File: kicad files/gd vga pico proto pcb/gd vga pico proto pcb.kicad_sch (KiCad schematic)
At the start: 58 parts, among them J1 RGB Bin, J2 CLKS, J3 SWD, J4 L77HDE15SD1CH4F, J5 VID_TXRX, J6 WIN, J7 5V, J8 USB_B_Micro, SW1 2040 RESET, U1 RP2040, U2 74HCT245, U3 74LVC2G04, U4 74LVC2G04, U5 MIC5504-3.3YM5, Y1 ECS-120-18-33-JEM-TR

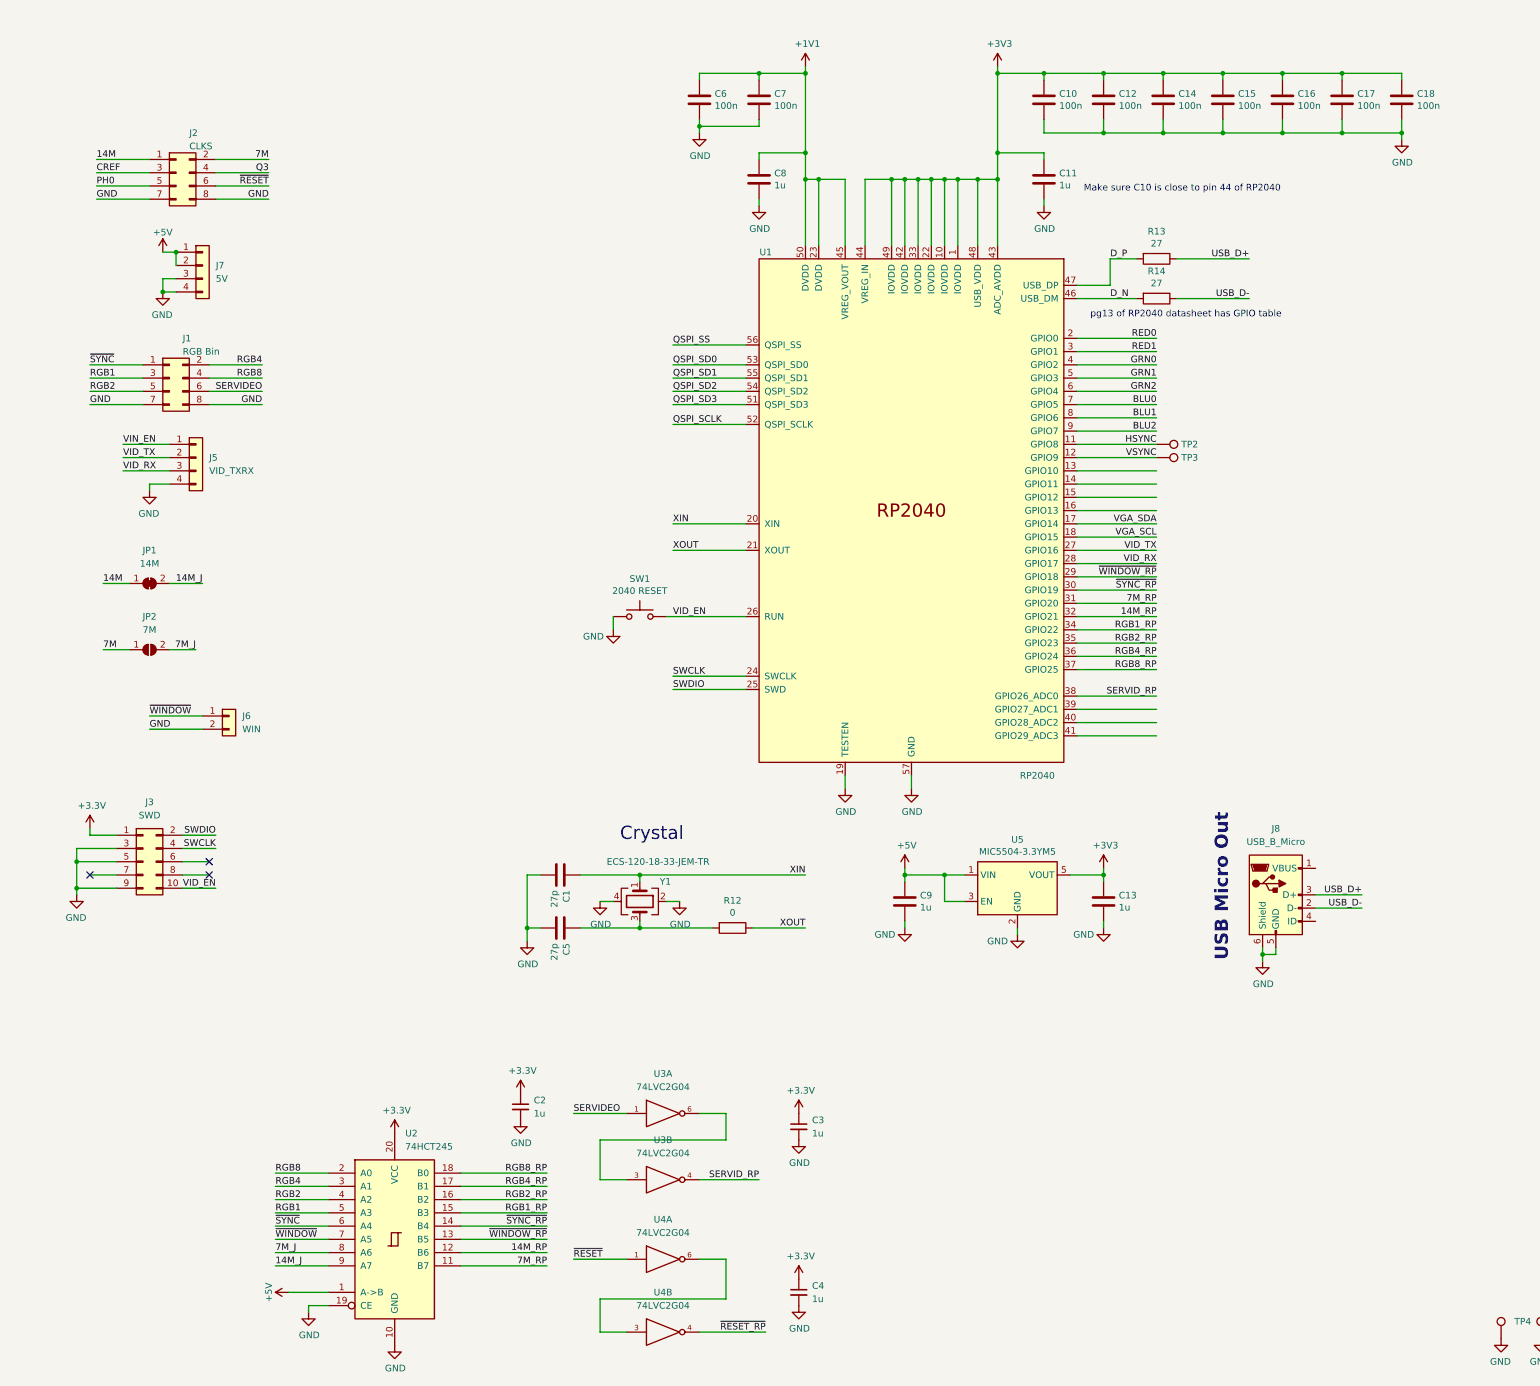
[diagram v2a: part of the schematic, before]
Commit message: post stream pixel pushing.
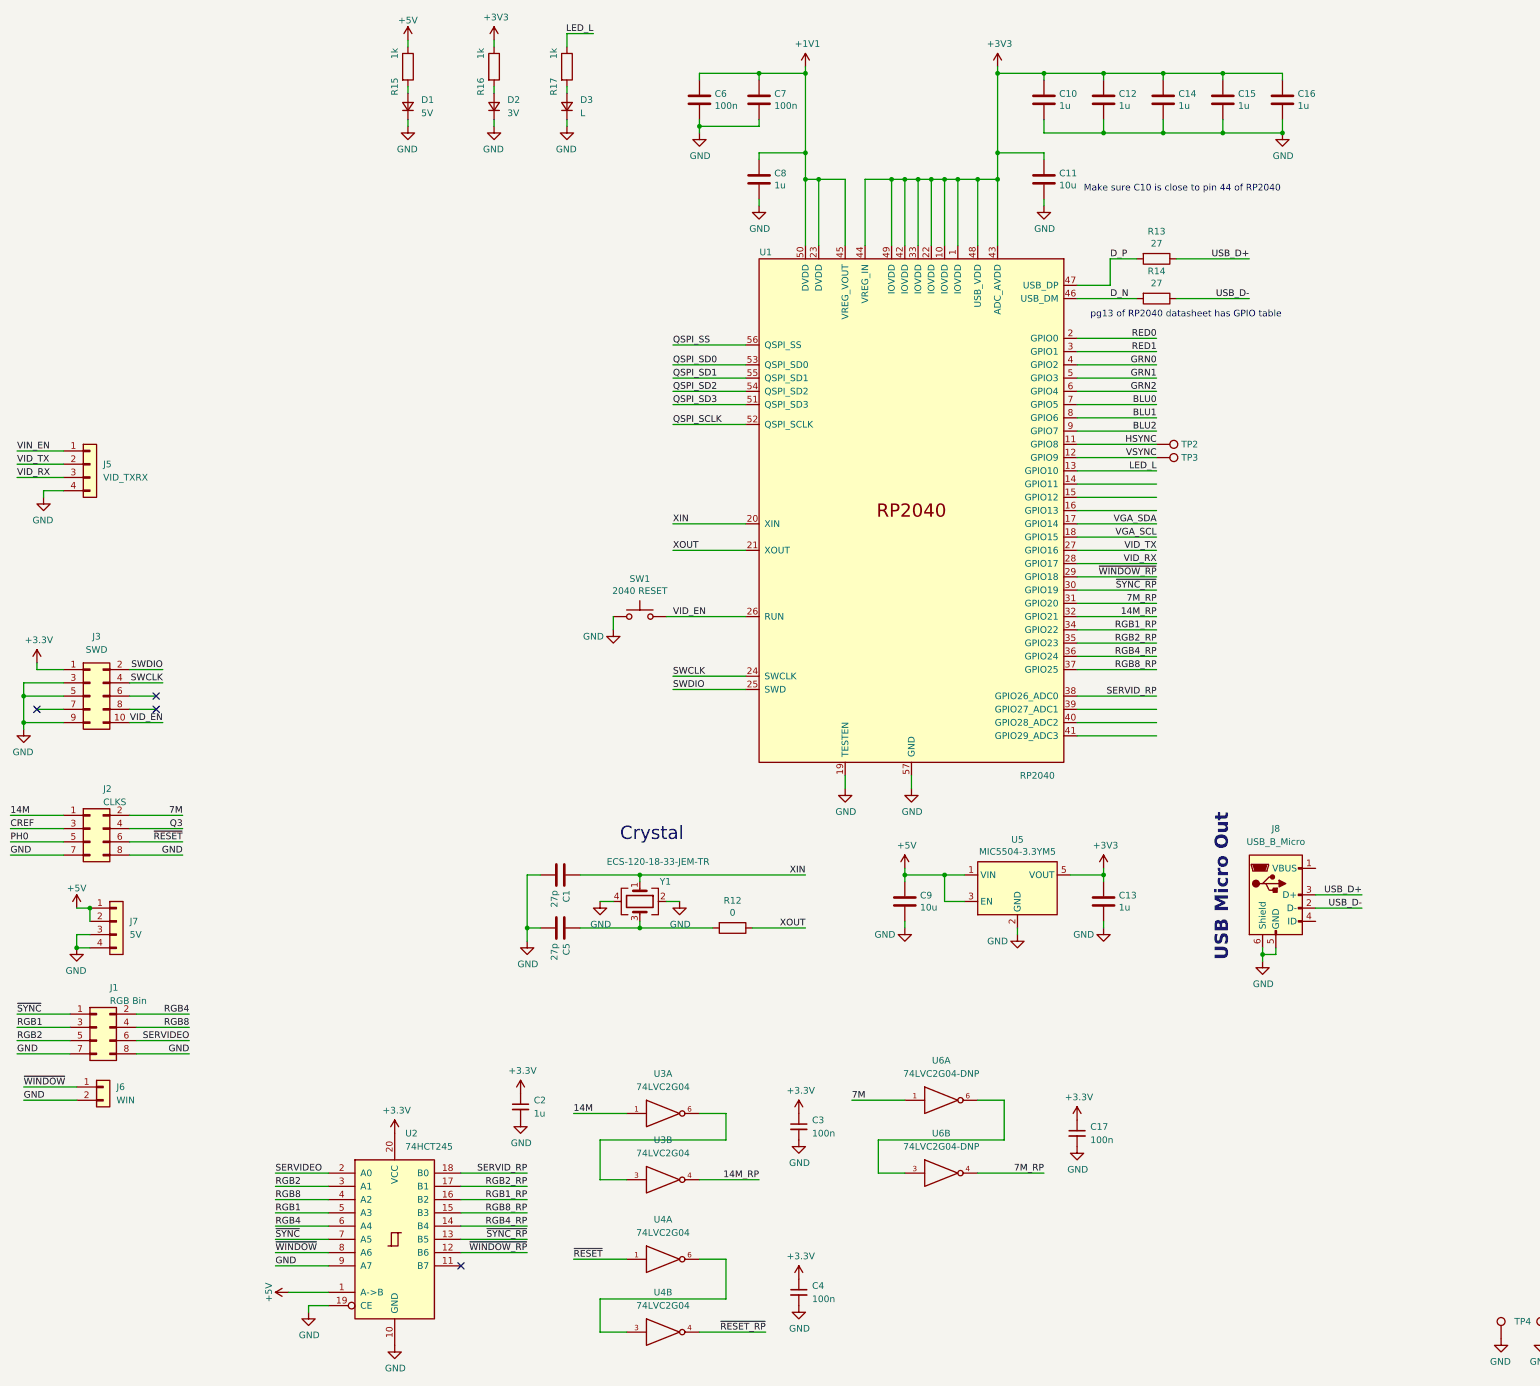
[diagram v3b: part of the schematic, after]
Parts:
- removed C17, C18: 100n, Capacitor_SMD:C_0603_1608Metric, symbol Device:C
- removed JP1: 14M, Jumper:SolderJumper-2_P1.3mm_Bridged_RoundedPad1.0x1.5mm, symbol Jumper:SolderJumper_2_Bridged
- removed JP2: 7M, Jumper:SolderJumper-2_P1.3mm_Open_TrianglePad1.0x1.5mm, symbol Jumper:SolderJumper_2_Open
- added C17: 100n, Capacitor_SMD:C_0603_1608Metric, symbol My Library:C_0805
- added D1: 5V, LED_SMD:LED_1206_3216Metric, symbol My Library:D_1206
- added D2: 3V, LED_SMD:LED_1206_3216Metric, symbol My Library:D_1206
- added D3: L, LED_SMD:LED_1206_3216Metric, symbol My Library:D_1206
- added R15, R16, R17: 1k, Resistor_SMD:R_0603_1608Metric, symbol Device:R
- added U6: 74LVC2G04-DNP, Package_TO_SOT_SMD:SOT-23-6, symbol 74xGxx:74LVC2G04
- C10, C12, C14, C15, C16: value 100n -> 1u
- C11: value 1u -> 10u; footprint Capacitor_SMD:C_0603_1608Metric -> Capacitor_SMD:C_0805_2012Metric
- C13, C2: footprint Capacitor_SMD:C_0805_2012Metric -> Capacitor_SMD:C_0603_1608Metric
- C3, C4: value 1u -> 100n; footprint Capacitor_SMD:C_0805_2012Metric -> Capacitor_SMD:C_0603_1608Metric
- C9: value 1u -> 10u
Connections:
- net +3.3V is gone; now on net +3V3: U3.5 (+3V3), U3.5 (+3V3), U4.5 (+3V3), U4.5 (+3V3)
- net 14M_J is gone; now on net GND: U2.9 (A7)
- net 7M_J is gone; now on net ~{WINDOW}: U2.8 (A6)
- net +3V3: now also C17.1, R16.1, U6.5 (+3V3), U6.5 (+3V3)
- net +5V: now also R15.1
- net 14M: now also U3.1
- net 14M_RP: now also U3.4; no longer U2.12 (B6)
- net 7M: now also U6.1
- net 7M_RP: now also U6.4; no longer U2.11 (B7)
- net GND: now also C17.2, D1.1 (K), D2.1 (K), D3.1 (K), U6.2 (GND), U6.2 (GND)
- net RGB1_RP: now also U2.16 (B2); no longer U2.15 (B3)
- net RGB2: now also U2.3 (A1); no longer U2.4 (A2)
- net RGB2_RP: now also U2.17 (B1); no longer U2.16 (B2)
- net RGB4: now also U2.6 (A4); no longer U2.3 (A1)
- net RGB4_RP: now also U2.14 (B4); no longer U2.17 (B1)
- net RGB8: now also U2.4 (A2); no longer U2.2 (A0)
- net RGB8_RP: now also U2.15 (B3); no longer U2.18 (B0)
- net SERVIDEO: now also U2.2 (A0); no longer U3.1
- net SERVID_RP: now also U2.18 (B0); no longer U3.4
- net ~{SYNC_RP}: now also U2.13 (B5); no longer U2.14 (B4)
- net ~{SYNC}: now also U2.7 (A5); no longer U2.6 (A4)
- net ~{WINDOW_RP}: now also U2.12 (B6); no longer U2.13 (B5)
- net ~{WINDOW}: no longer U2.7 (A5)
- net LED_L: now reaches U1.13 (GPIO10)
- net LED_L: now also R17.1
- new net: D2.2 (A), R16.2
- new net: D1.2 (A), R15.2
- new net: D3.2 (A), R17.2
- new net: U6.3, U6.6
- no-connect marks 5 -> 6
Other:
- moved on the sheet: J1, J2, J3, J5, J6, J7

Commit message: rev1 finish from stream, need final review
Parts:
- removed C15: 1u, Capacitor_SMD:C_0603_1608Metric, symbol Device:C
- removed C7: 100n, Capacitor_SMD:C_0603_1608Metric, symbol Device:C
- added C18: 100n, Capacitor_SMD:C_0805_2012Metric, symbol Device:C
- added U7: W25Q128JVS, Package_SO:SOIC-8_5.23x5.23mm_P1.27mm, symbol Memory_Flash:W25Q128JVS
- C1, C5: value 27p -> 6p; footprint Capacitor_SMD:C_0603_1608Metric -> Capacitor_SMD:C_0402_1005Metric
- C6: value 100n -> 1u
- J3: footprint Connector_PinSocket_1.27mm:PinSocket_2x05_P1.27mm_Vertical_SMD -> FTSH-105-01-L-DV-K:SAMTEC_FTSH-105-XX-X-DV; symbol Connector_Generic:Conn_02x05_Odd_Even -> FTSH-105-XX-X-DV:FTSH-105-XX-X-DV; MANUFACTURER (none) -> Samtec; PARTREV (none) -> H; STANDARD (none) -> Manufacturer Recommendation
- J4: footprint Connector_Dsub:DSUB-15-HD_Female_Horizontal_P2.29x1.98mm_EdgePinOffset8.35mm_Housed_MountingHolesOffset10.89mm -> L77HDE15SD1CH4F:AMPHENOL_L77HDE15SD1CH4F
- Y1: value ECS-120-18-33-JEM-TR -> ABM10AIG-12.000MHZ-7-D2Z-T; footprint Crystal:Crystal_SMD_3225-4Pin_3.2x2.5mm -> Crystal:Crystal_SMD_2520-4Pin_2.5x2.0mm; Old PN ABLS-12.000MHZ-B4-T -> (none)
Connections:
- net VIN_EN is gone; now on net VID_EN: J5.1 (Pin_1)
- net +3V3: now also J3.01, U2.1 (A->B), C18.1, U7.8 (VCC); no longer J3.1 (Pin_1)
- net +5V: no longer U2.1 (A->B)
- net 14M_RP: now also U1.16 (GPIO13); no longer U1.32 (GPIO21)
- net 7M_RP: now also U1.15 (GPIO12); no longer U1.31 (GPIO20)
- net BLU0: now also U1.36 (GPIO24); no longer U1.7 (GPIO5)
- net BLU1: now also U1.35 (GPIO23); no longer U1.8 (GPIO6)
- net BLU2: now also U1.34 (GPIO22); no longer U1.9 (GPIO7)
- net GND: now also J3.03, J3.05, J3.09, C18.2, U7.4 (GND); no longer J3.3 (Pin_3), J3.5 (Pin_5), J3.9 (Pin_9)
- net GRN0: now also U1.39 (GPIO27_ADC1); no longer U1.4 (GPIO2)
- net GRN1: now also U1.38 (GPIO26_ADC0); no longer U1.5 (GPIO3)
- net GRN2: now also U1.37 (GPIO25); no longer U1.6 (GPIO4)
- net HSYNC: now also U1.32 (GPIO21); no longer U1.11 (GPIO8)
- net LED_L: now also U1.5 (GPIO3); no longer U1.13 (GPIO10)
- net QSPI_SCLK: now also U7.6 (CLK)
- net QSPI_SD0: now also U7.5 (DI(IO0))
- net QSPI_SD1: now also U7.2 (DO(IO1))
- net QSPI_SD2: now also U7.3 (IO2)
- net QSPI_SD3: now also U7.7 (IO3)
- net QSPI_SS: now also U7.1 (~{CS})
- net RED0: now also U1.41 (GPIO29_ADC3); no longer U1.2 (GPIO0)
- net RED1: now also U1.40 (GPIO28_ADC2); no longer U1.3 (GPIO1)
- net RGB1_RP: now also U1.18 (GPIO15); no longer U1.34 (GPIO22)
- net RGB2_RP: now also U1.17 (GPIO14); no longer U1.35 (GPIO23)
- net RGB4_RP: now also U1.28 (GPIO17); no longer U1.36 (GPIO24)
- net RGB8_RP: now also U1.27 (GPIO16); no longer U1.37 (GPIO25)
- net SERVID_RP: now also U1.14 (GPIO11); no longer U1.38 (GPIO26_ADC0)
- net SWCLK: now also J3.04; no longer J3.4 (Pin_4)
- net SWDIO: now also J3.02; no longer J3.2 (Pin_2)
- net VGA_SCL: no longer U1.18 (GPIO15)
- net VGA_SDA: no longer U1.17 (GPIO14)
- net VID_RX: now also U1.7 (GPIO5); no longer U1.28 (GPIO17)
- net VID_TX: now also U1.6 (GPIO4); no longer U1.27 (GPIO16)
- net VSYNC: now also U1.31 (GPIO20); no longer U1.12 (GPIO9)
- net ~{RESET_RP}: now also U1.13 (GPIO10)
- net ~{SYNC_RP}: now also U1.29 (GPIO18); no longer U1.30 (GPIO19)
- net ~{WINDOW_RP}: now also U1.30 (GPIO19); no longer U1.29 (GPIO18)
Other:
- note added: "${board_name} rev ${REVISION}, ${ISSUE_DATE} @baldengineer"
- note added: "Flash"
- moved on the sheet: C6, J3, TP2, TP3
